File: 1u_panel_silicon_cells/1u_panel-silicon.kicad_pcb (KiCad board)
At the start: 2 copper layers, 83 x 100 mm, 137 parts, among them J1 MMS-104-01-[F/L]-SH, J2 2-1734592-0, Q1 DMP3050LVT-7, Q2 DMP2240UDM-7, U1 TCAN330GDCNT, U10 TPS63060DSCR, U11 TMP101NA/3KSLOTTED, U12 LTC4412, U13 LTC4411, U14 LTC4411, U15 LTC4411, U16 LTC4411, U2 TMP101NA/3KSLOTTED, U3 LT1618EMSTRPBF, U4 INA226, U5 LTC4411, U6 LTC4411, U7 STM32F091CCT7, U8 LTC4411, U9 LTC4411, X1 ECS-160-10-36Q-ES-TR

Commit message: changes for silicon solar module bringup tasks
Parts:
- removed R34, R35: 100, oresat-passives:0603-C-NOSILK
- removed TP5: TEST-POINT-LARGE-SQUARE, oresat-misc:TestPoint-0.75mm-th
- added C37: 100n, oresat-passives:0603-C-NOSILK, F.Cu at (138.8, 71.8)
- D12, D13: value KXOB2502X8F -> KXOB2502X8TF; footprint oresat-misc:KXOB2502X8F -> oresat-misc:KXOB2502X8TF
- Q1: value DMP3050LVT-7 -> NTR4101P; footprint Package_TO_SOT_SMD:SOT-23-6 -> Package_TO_SOT_SMD:SOT-23
- R36, R37: value 100 -> 10
- U3: footprint Package_SO:MSOP-10_3x3mm_P0.5mm -> oresat-ics:MSOP-10_MS
- moved TP12 2.00 mm to (155.9, 77.6)
- moved U4 1.40 mm to (137.8, 67.6)
- moved C8 1.30 mm to (135.4, 70.6)
- moved TP24 1.30 mm to (137.8, 62.2)
- moved TP11 0.30 mm to (144.5, 67.7)
- moved Q1 0.10 mm to (144.3, 70.5), turned to 90 degrees
- turned R36 to 90 degrees
- turned U11 to 0 degrees
- turned U2 to 0 degrees
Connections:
- L2 pad 1: Net-(L2-Pad1) -> Net-(U3-ISN)
- Q1 pad 1: /1u_panel-power/VMPPT -> /1u_panel-power/~{SHDN-OUPUT}
- Q1 pad 3: /1u_panel-power/~{SHDN-OUPUT} -> Net-(Q1-D)
- R17 pad 2: Net-(L2-Pad1) -> Net-(U3-ISN)
- R36 pad 1: Net-(U4-Vin-) -> Net-(U3-ISN)
- R36 pad 2: Net-(L2-Pad1) -> Net-(U4-Vbus)
- R37 pad 1: Net-(U4-Vbus) -> Net-(U4-Vin+)
- U11 pad 1: 3.3V -> SCL
- U11 pad 2: 3.3V -> GND
- U11 pad 3: SDA -> Net-(U11-ALERT)
- U11 pad 4: SCL -> 3.3V
- U11 pad 5: GND -> 3.3V
- U11 pad 6: Net-(U11-ALERT) -> SDA
- U12 pad 3: Net-(Q1-S) -> Net-(Q1-D)
- U2 pad 1: 3.3V -> SCL
- U2 pad 3: SDA -> Net-(U2-ALERT)
- U2 pad 4: SCL -> 3.3V
- U2 pad 6: Net-(U2-ALERT) -> SDA
- U3 pad 3: Net-(U3-ISP) -> VSOLAR
- U4 pad 10: Net-(U4-Vbus) -> Net-(U4-Vin+)
- U4 pad 4: SCL -> SDA
- U4 pad 5: SDA -> SCL
- U4 pad 9: Net-(U4-Vin-) -> Net-(U4-Vbus)
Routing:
- net Net-(L2-Pad1): track 18.4 -> 0.00 mm
- net Net-(Q1-S): track 10.0 -> 0.00 mm, vias 2 -> 0
- net Net-(Q1-D): track 0.00 -> 8.14 mm, vias 0 -> 2
- net Net-(U3-ISN): track 2.86 -> 8.65 mm
- net VSOLAR: track 203.3 -> 208.3 mm
- net Net-(U4-Vin+): track 0.00 -> 4.56 mm
- net /1u_panel-power/VMPPT: track 26.9 -> 22.6 mm
- net Net-(U3-ISP): track 4.00 -> 0.00 mm
- net Net-(U4-Vin-): track 3.83 -> 0.00 mm
- net Net-(U4-Vbus): track 5.79 -> 7.83 mm
- net /1u_panel-power/~{SHUTDOWN}: track 69.6 -> 71.6 mm
- net SCL: track 180.7 -> 182.5 mm
- net /1u_panel-power/~{SHDN-OUPUT}: track 9.22 -> 7.93 mm
- net Net-(D5-ANODE): track 5.82 -> 6.64 mm
- net GND: vias 1118 -> 1115
- added copper zone on F.Cu, net Net-(U3-ISN)
- removed copper zone on F.Cu, net Net-(L2-Pad1)
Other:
- board text added: "2025/01/29"
- board text added: "OreSat Si-Solar Module v1.1"
- board text added: "SN:"
- board text removed: "2024/09/13"
- board text removed: "OreSat Si-Solar Module v1.0"

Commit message: chages for https://github.com/oresat/oresat-solar-hardware/issues/53
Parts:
- removed TP26, TP27, TP28, TP29: TEST-POINT-LARGE-SQUARE, oresat-misc:TestPoint-0.75mm-th
- added C38: 1u, oresat-passives:0603-C-NOSILK, F.Cu at (128.1, 94.3)
- added C39: 4.7u, oresat-passives:0603-C-NOSILK, F.Cu at (140.7, 95.1)
- added C40: 4.7u, oresat-passives:0603-C-NOSILK, F.Cu at (159.7, 98.1)
- added C41: 4.7u, oresat-passives:0603-C-NOSILK, F.Cu at (124.4, 119.3)
- added C42: 4.7u, oresat-passives:0603-C-NOSILK, F.Cu at (142.5, 121.8)
- added C43: 4.7u, oresat-passives:0603-C-NOSILK, F.Cu at (178.8, 115.1)
- added C44: 4.7u, oresat-passives:0603-C-NOSILK, F.Cu at (171.9, 102.6)
- added C45: 4.7u, oresat-passives:0603-C-NOSILK, F.Cu at (140.9, 106.4)
- added TP17: TEST-POINT-LARGE-SQUARE, oresat-misc:TestPoint-0.75mm-th, F.Cu at (171.9, 111.1)
- added TP18: TEST-POINT-LARGE-SQUARE, oresat-misc:TestPoint-0.75mm-th, F.Cu at (139.1, 80.3)
- added TP5: TEST-POINT-LARGE-SQUARE, oresat-misc:TestPoint-0.75mm-th, F.Cu at (125.2, 111.0)
- added TP8: TEST-POINT-LARGE-SQUARE, oresat-misc:TestPoint-0.75mm-th, F.Cu at (185.1, 81.9)
- C10: value 1u -> 4.7u
- R17: value 0.1 -> 100m; footprint oresat-passives:0805-C-NOSILK -> oresat-passives:1206-C
- U1: footprint oresat-ics:SOT23-8_TI-DCN -> Package_TO_SOT_SMD:SOT-23-8
- moved C10 5.32 mm to (127.5, 88.2)
- moved U8 1.20 mm to (159.7, 94.2)
- moved L2 1.20 mm to (145.2, 76.6)
- moved R28 1.14 mm to (159.7, 96.8)
- moved C24 1.14 mm to (162.6, 94.5)
- moved R10 1.10 mm to (150.8, 78.1)
- moved R16 1.10 mm to (149.3, 79.2)
- moved C2 1.10 mm to (151.5, 79.2)
- moved TP7 1.01 mm to (185.0, 79.8)
- moved U5 1.00 mm to (128.3, 91.6)
- moved C18 1.00 mm to (153.4, 77.3)
- moved D5 1.00 mm to (150.4, 76.6)
- moved R12 1.00 mm to (151.4, 80.9)
- moved R32 1.00 mm to (171.9, 104.0)
- moved R7 1.00 mm to (149.7, 82.1)
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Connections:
- C10 pad 1: Net-(D2-A1) -> VSOLAR
- C37 pad 1: Net-(U4-Vin+) -> Net-(U4-Vbus)
- C37 pad 2: Net-(U4-Vbus) -> Net-(U4-Vin-)
- R36 pad 2: Net-(U4-Vbus) -> Net-(U4-Vin-)
- R37 pad 1: Net-(U4-Vin+) -> Net-(U4-Vbus)
- U4 pad 10: Net-(U4-Vin+) -> Net-(U4-Vbus)
- U4 pad 9: Net-(U4-Vbus) -> Net-(U4-Vin-)
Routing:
- net Net-(U4-Vin-): track 0.00 -> 7.49 mm
- net Net-(U4-Vin+): track 4.56 -> 0.00 mm
- net SDA: track 185.1 -> 181.6 mm
- net VSOLAR: track 208.3 -> 205.0 mm, vias 17 -> 15
- net Net-(U10-VAUX): track 4.58 -> 1.67 mm
- net SCL: track 182.5 -> 179.6 mm
- net Net-(D12-A1): track 3.20 -> 5.41 mm
- net /1u_panel-power/~{SHUTDOWN}: track 71.6 -> 69.5 mm
- net 3.3V: track 249.8 -> 248.2 mm
- net LT1618-IADJ: track 47.9 -> 46.5 mm
- net Net-(U10-FB): track 6.49 -> 5.19 mm
- net Net-(D8-A1): track 5.45 -> 6.63 mm
- net Net-(Q1-D): track 8.14 -> 9.32 mm
- net LT1618-ENABLE: track 40.8 -> 39.7 mm
- net Net-(U4-Vbus): track 7.83 -> 6.78 mm
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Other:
- board text added: "GND"
- board text added: "TP17"
- board text added: "TP5"

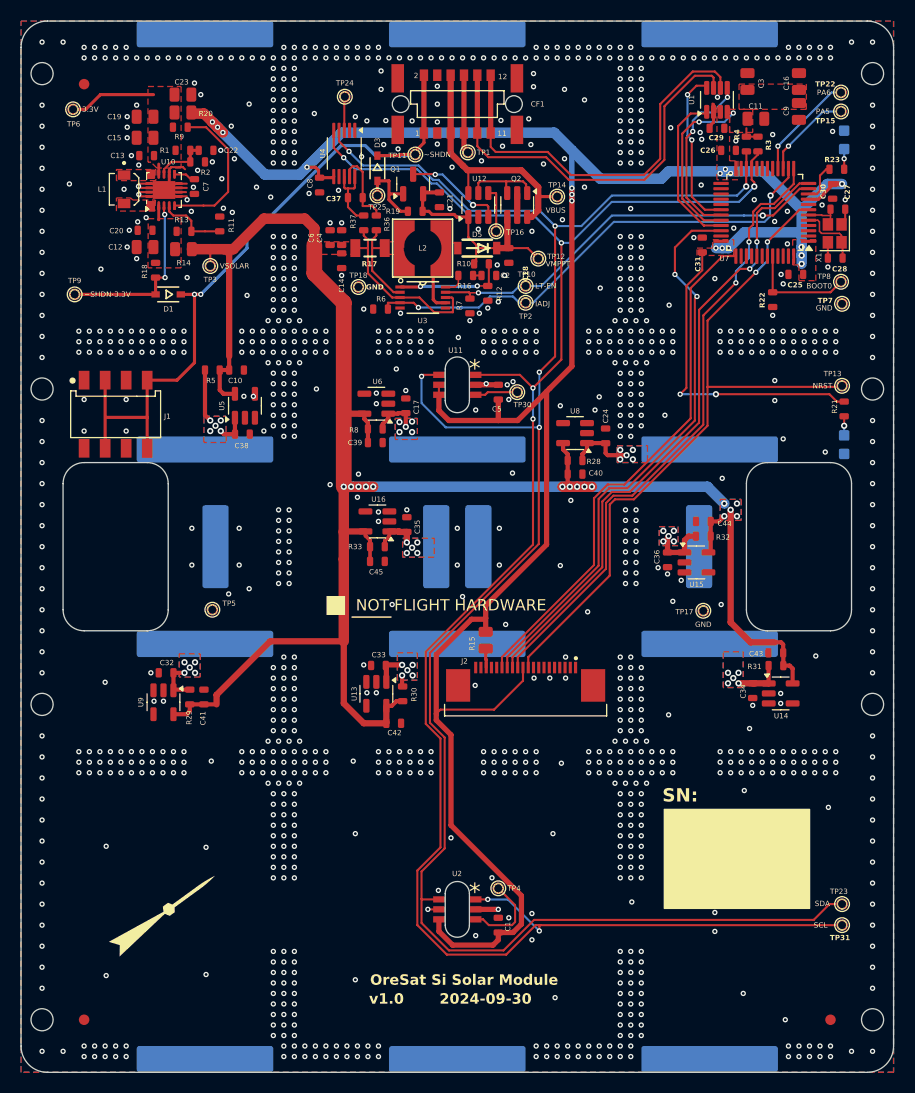
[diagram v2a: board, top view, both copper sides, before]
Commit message: changes for bringup issues on Si Solar module
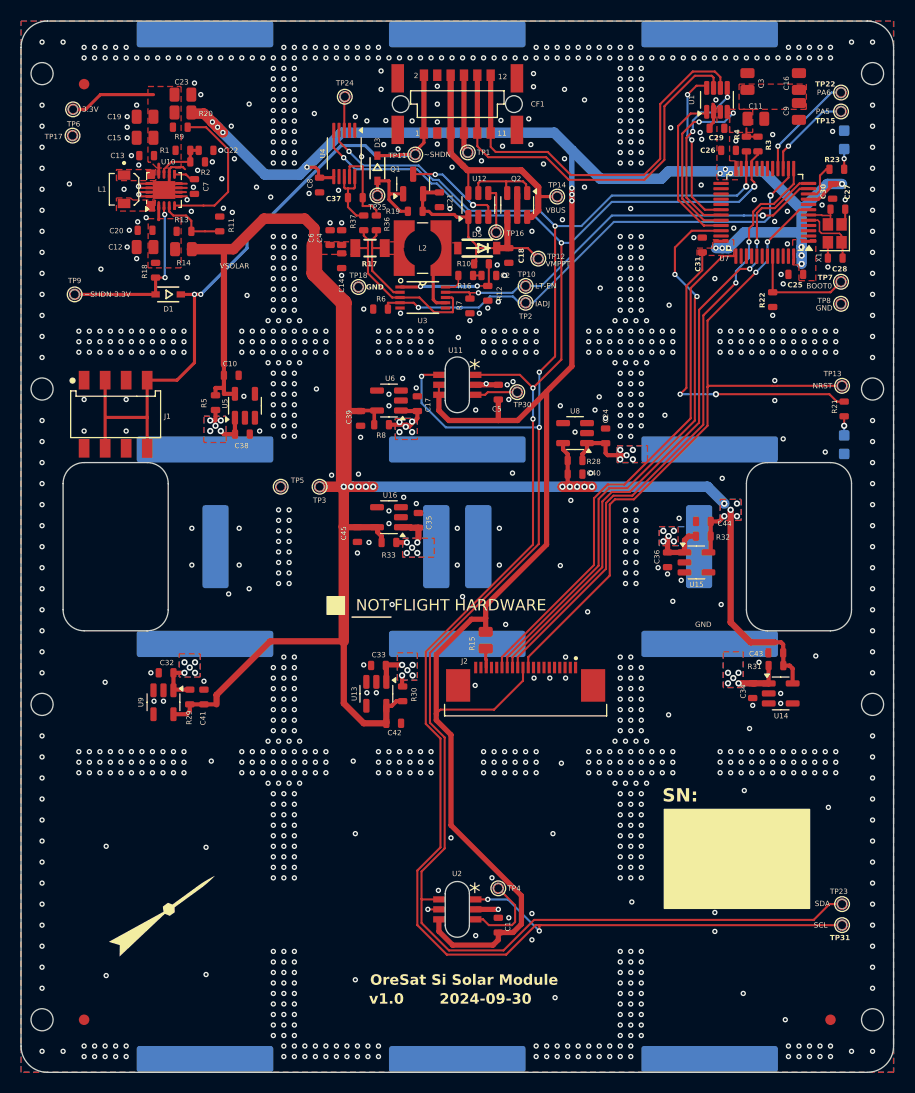
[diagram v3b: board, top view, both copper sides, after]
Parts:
- moved TP17 75.1 mm to (111.9, 65.9)
- moved TP3 23.4 mm to (135.4, 99.3)
- moved TP5 13.4 mm to (131.7, 99.3)
- moved C45 3.18 mm to (139.0, 103.8), turned to -90 degrees
- moved R5 3.11 mm to (125.5, 91.3), turned to 90 degrees
- moved C39 2.69 mm to (139.3, 92.8), turned to -90 degrees
- moved U6 1.24 mm to (142.0, 91.1)
- moved C35 1.17 mm to (144.8, 102.5)
- moved R33 1.17 mm to (142.0, 104.6)
- moved U16 1.17 mm to (142.0, 102.2)
- moved C17 1.12 mm to (144.7, 91.4)
- moved R8 0.72 mm to (141.3, 93.4)
- moved C10 0.71 mm to (127.0, 88.7)
- moved TP16 0.10 mm to (152.2, 75.1)
- moved TP8 0.10 mm to (185.0, 81.9)
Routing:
- net Net-(D2-A1): track 8.01 -> 4.51 mm
- net Net-(D7-A1): track 7.41 -> 8.52 mm
- net Net-(D13-A1): track 4.31 -> 3.61 mm
- net unconnected-(U5-Pad4): vias 1 -> 0
- net GND: vias 1133 -> 1142

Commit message: Cleanup before fab! Added pullup resistors to ALERTs on TMP101s, removed some paranoia hardware including test points and pullups we don't need, did some schematic polishing for prettiness, and cleaned up some of the zones onthe layout. Removed the need for any old import or local symbol or footprint libraries. Upgraded to v1.1.
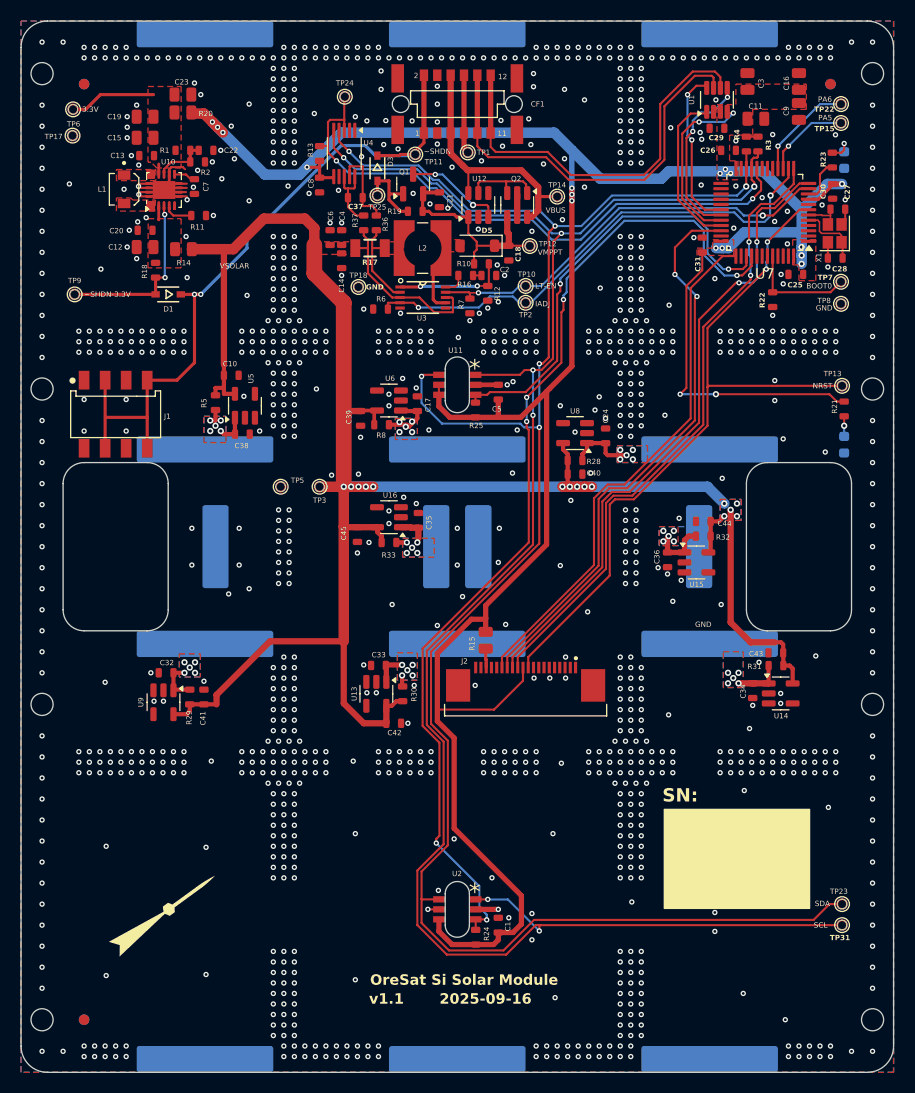
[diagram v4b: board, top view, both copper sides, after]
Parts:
- removed R9: 1M, oresat-passives:0603-C-NOSILK
- removed TP16, TP30, TP4: TEST-POINT-LARGE-SQUARE, oresat-misc:TestPoint-0.75mm-th
- removed U$1: FLIGHMARKERNEW, oresat-graphics:FLIGHTMARKER_NEW_BOARDS
- removed U$2, U$3, U$4: FIDUCIAL, Fiducial:Fiducial_1mm_Mask2mm
- added FID1: Fiducial, Fiducial:Fiducial_1mm_Mask2mm, F.Cu at (113.0, 61.0)
- added FID2: Fiducial, Fiducial:Fiducial_1mm_Mask2mm, F.Cu at (184.0, 61.0)
- added FID3: Fiducial, Fiducial:Fiducial_1mm_Mask2mm, F.Cu at (113.0, 150.0)
- added FID4: Fiducial, Fiducial:Fiducial_1mm_Mask2mm, B.Cu at (113.0, 61.0)
- added FID5: Fiducial, Fiducial:Fiducial_1mm_Mask2mm, B.Cu at (184.0, 61.0)
- added FID6: Fiducial, Fiducial:Fiducial_1mm_Mask2mm, B.Cu at (113.0, 150.0)
- added R24: 10k, oresat-passives:0603-C-NOSILK, F.Cu at (150.2, 142.2)
- added R25: 10k, oresat-passives:0603-C-NOSILK, F.Cu at (150.2, 92.0)
- D4: value GREEN -> GRN; footprint oresat-diodes:LED-0603 -> LED_SMD:LED_0603_1608Metric
- D5: footprint oresat-diodes:SOD123 -> Diode_SMD:D_SOD-123
- D6: footprint oresat-diodes:LED-0603 -> LED_SMD:LED_0603_1608Metric
- R13: value NP -> 10k
- U1: value TCAN330GDCNT -> TCAN330
- moved R13 14.9 mm to (135.4, 67.6), turned to -90 degrees
- moved R11 2.16 mm to (123.9, 73.5), turned to 180 degrees
- moved D6 1.92 mm to (185.3, 68.2)
- moved TP12 1.44 mm to (155.4, 76.4)
- moved TP15 1.10 mm to (185.0, 64.7)
- moved TP22 1.10 mm to (185.0, 62.9)
- moved R23 0.97 mm to (184.2, 68.2), turned to -90 degrees
- moved C18 0.22 mm to (153.4, 77.1)
- moved D5 0.22 mm to (150.4, 76.4)
- turned D4 to 90 degrees
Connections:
- L2 pad 2: Net-(D5-ANODE) -> Net-(D5-A)
- R13 pad 1: Net-(U10-PS/SYNC) -> INA226-nALERT
- R13 pad 2: Net-(U10-VIN) -> 3.3V
- R21 pad 2: Net-(D4-PadA) -> Net-(D4-A)
- TP24 pad 1: Net-(U4-~{Alert}) -> INA226-nALERT
- U10 pad 5: Net-(U10-PG) -> unconnected-(U10-PG-Pad5)_1
- U12 pad 4: Net-(U12-STAT) -> unconnected-(U12-STAT-Pad4)
- U3 pad 7: Net-(D5-ANODE) -> Net-(D5-A)
- U4 pad 3: Net-(U4-~{Alert}) -> INA226-nALERT
- U7 pad 20: unconnected-(U7-PB2-Pad20) -> INA226-nALERT
- U7 pad 39: unconnected-(U7-PB3-Pad39) -> Net-(U11-ALERT)
- U7 pad 40: unconnected-(U7-PB4-Pad40) -> Net-(U2-ALERT)
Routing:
- net Net-(U2-ALERT): track 7.97 -> 96.4 mm, vias 0 -> 6
- net INA226-nALERT: track 0.00 -> 57.4 mm, vias 0 -> 2
- net Net-(U11-ALERT): track 4.05 -> 42.4 mm, vias 0 -> 2
- net Net-(U10-PG): track 14.4 -> 0.00 mm
- net Net-(D5-ANODE): track 5.70 -> 0.00 mm
- net Net-(D5-A): track 0.00 -> 5.70 mm
- net Net-(U12-STAT): track 4.36 -> 0.00 mm
- net Net-(U10-PS/SYNC): track 6.74 -> 2.83 mm
- net Net-(U4-~{Alert}): track 3.22 -> 0.00 mm
- net GND: track 21.3 -> 19.0 mm, vias 1142 -> 1144
- net Net-(D4-PadA): track 1.82 -> 0.00 mm, vias 1 -> 0
- net Net-(D4-A): track 0.00 -> 1.82 mm, vias 0 -> 1
- net /1u_panel-power/VMPPT: track 22.0 -> 20.6 mm
- net 3.3V: track 248.2 -> 247.1 mm
- net LT1618-IADJ: track 46.5 -> 47.2 mm
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- added copper zone on F.Cu, net Net-(D5-A)
- removed copper zone on F.Cu, net Net-(D5-ANODE)
